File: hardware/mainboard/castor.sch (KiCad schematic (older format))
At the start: 41 parts, among them Q1 MMBT3904, U3 TL074, U4 74LVC2G74, U5 MCP6001-OT, U6 TL074

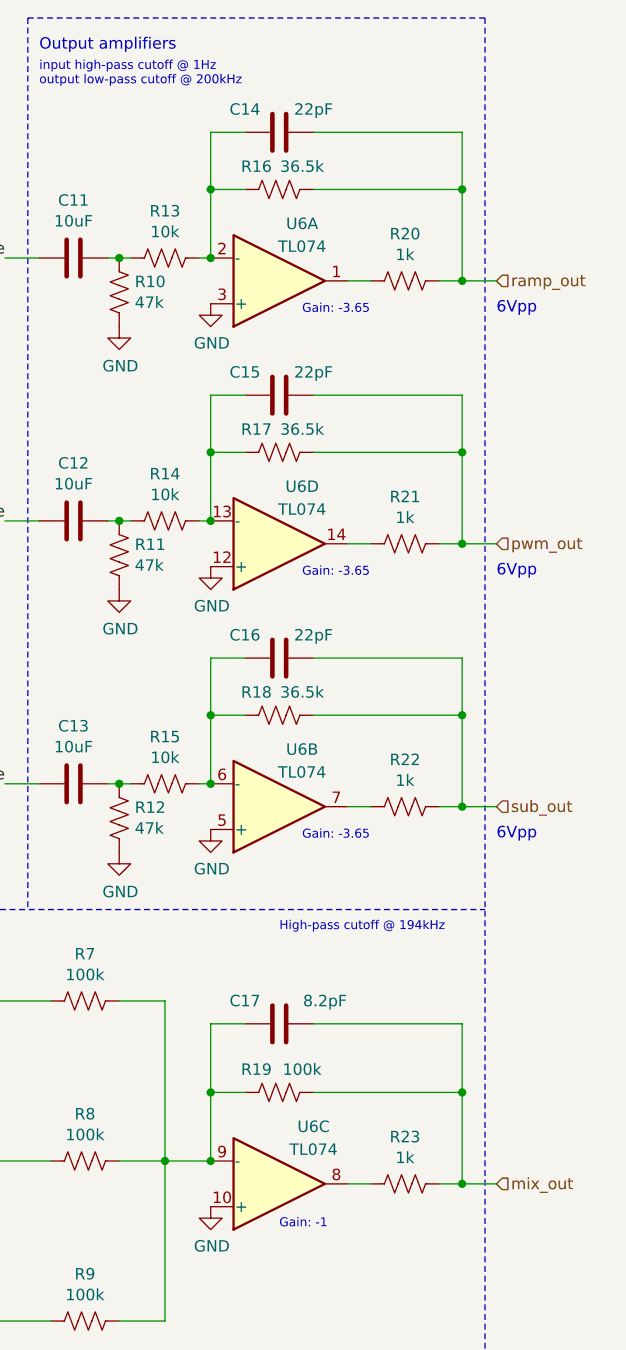
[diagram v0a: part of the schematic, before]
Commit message: Move output resistors outside of the feedback loop
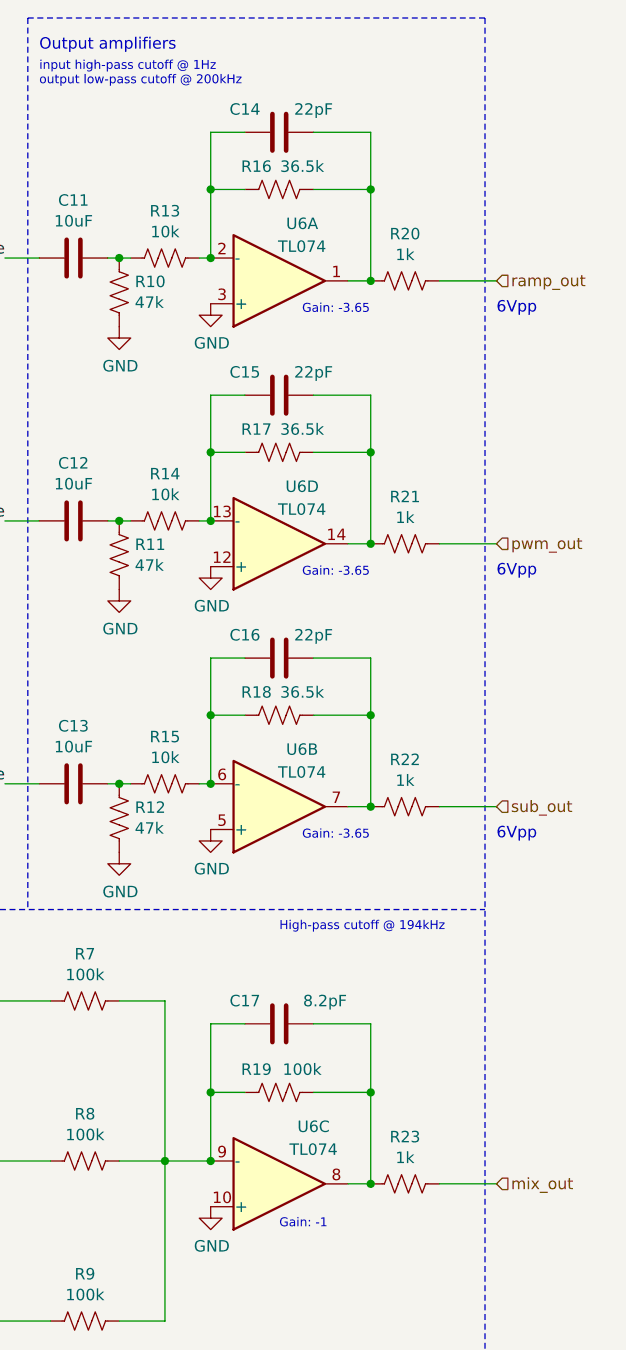
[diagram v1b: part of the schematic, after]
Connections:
- net mix_out: no longer C17.1, R19.2
- net pwm_out: no longer C15.1, R17.2
- net ramp_out: no longer C14.1, R16.2
- net sub_out: no longer C16.1, R18.2
- net at R20.1, U6.1: now also C14.1, R16.2
- net at R23.1, U6.8: now also C17.1, R19.2
- net at R21.1, U6.14: now also C15.1, R17.2
- net at R22.1, U6.7: now also C16.1, R18.2
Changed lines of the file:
@@
 	8550 5200 8700 5200
 Wire Wire Line
-	9000 5200 9650 5200
+	9000 5200 9250 5200
 $Comp
 L Device:R_US R7
@@
 $EndComp
 Wire Wire Line
-	9550 1650 9650 1650
-Wire Wire Line
 	8550 1550 8550 1250
 Wire Wire Line
@@
 Connection ~ 8550 1550
 Wire Wire Line
-	9000 1000 9650 1000
-Wire Wire Line
-	9650 1000 9650 1250
-Connection ~ 9650 1650
-Wire Wire Line
-	9650 1650 9800 1650
+	9000 1000 9250 1000
 Wire Wire Line
 	8550 1250 8700 1250
@@
 	8550 1250 8550 1000
 Wire Wire Line
-	9000 1250 9650 1250
-Connection ~ 9650 1250
-Wire Wire Line
-	9650 1250 9650 1650
+	9000 1250 9250 1250
 $Comp
 L Device:C C12
@@
 $EndComp
 Wire Wire Line
-	9550 2800 9650 2800
-Wire Wire Line
 	8550 2700 8550 2400
 Wire Wire Line
@@
 Connection ~ 8550 2700
 Wire Wire Line
-	9000 2150 9650 2150
-Wire Wire Line
-	9650 2150 9650 2400
-Connection ~ 9650 2800
-Wire Wire Line
-	9650 2800 9800 2800
+	9000 2150 9250 2150
 Wire Wire Line
 	8550 2400 8700 2400
@@
 	8550 2400 8550 2150
 Wire Wire Line
-	9000 2400 9650 2400
-Connection ~ 9650 2400
-Wire Wire Line
-	9650 2400 9650 2800
+	9000 2400 9250 2400
 Wire Notes Line
 	9750 500  7750 500
@@
 Connection ~ 8550 5200
 Wire Wire Line
-	9000 4900 9650 4900
-Wire Wire Line
-	9650 4900 9650 5200
+	9000 4900 9250 4900
 Wire Wire Line
 	8550 5500 8550 5200
-Wire Wire Line
-	9550 5600 9650 5600
-Wire Wire Line
-	9650 5200 9650 5600
-Connection ~ 9650 5200
-Connection ~ 9650 5600
-Wire Wire Line
-	9650 5600 9800 5600
 $Comp
 L power:GND #PWR016
@@
 	7750 500  7750 4400
 Wire Wire Line
-	9650 3550 9650 3950
-Connection ~ 9650 3550
-Wire Wire Line
-	9000 3550 9650 3550
+	9000 3550 9250 3550
 Wire Wire Line
 	8550 3550 8550 3300
@@
 	8550 3550 8700 3550
 Wire Wire Line
-	9650 3950 9800 3950
-Connection ~ 9650 3950
-Wire Wire Line
-	9650 3300 9650 3550
-Wire Wire Line
-	9000 3300 9650 3300
+	9000 3300 9250 3300
 Connection ~ 8550 3850
 Wire Wire Line
@@
 Wire Wire Line
 	8550 3850 8550 3550
-Wire Wire Line
-	9550 3950 9650 3950
 $Comp
 L Amplifier_Operational:TL074 U6
@@
 Text Notes 2050 4700 0    50   ~ 0
 1mA (max, est)
+Wire Wire Line
+	9250 1650 9250 1250
+Connection ~ 9250 1650
+Connection ~ 9250 1250
+Wire Wire Line
+	9250 1250 9250 1000
+Wire Wire Line
+	9550 1650 9800 1650
+Wire Wire Line
+	9250 2800 9250 2400
+Connection ~ 9250 2800
+Connection ~ 9250 2400
+Wire Wire Line
+	9250 2400 9250 2150
+Wire Wire Line
+	9550 2800 9800 2800
+Wire Wire Line
+	9250 3950 9250 3550
+Connection ~ 9250 3950
+Connection ~ 9250 3550
+Wire Wire Line
+	9250 3550 9250 3300
+Wire Wire Line
+	9550 3950 9800 3950
+Wire Wire Line
+	9250 5600 9250 5200
+Connection ~ 9250 5600
+Connection ~ 9250 5200
+Wire Wire Line
+	9250 5200 9250 4900
+Wire Wire Line
+	9550 5600 9800 5600
 $EndSCHEMATC

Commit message: Update mpns
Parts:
- C6, C9: mpn C0603C472F5GACTU -> C0603C472F3GECTU; mpn alt C0603C472F3GECTU -> C0603C472F5GACTU
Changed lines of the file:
@@
 F 4 "C0G 1%" H 2350 1250 50  0001 C CNN "Reqs"
 F 5 "yes" H 2350 1250 50  0001 C CNN "finalized"
-F 6 "C0603C472F5GACTU" H 2350 1250 50  0001 C CNN "mpn"
+F 6 "C0603C472F3GECTU" H 2350 1250 50  0001 C CNN "mpn"
 F 7 "1%, 50v" H 2350 1250 50  0001 C CNN "mpn specs"
-F 8 "C0603C472F3GECTU" H 2350 1250 50  0001 C CNN "mpn alt"
+F 8 "C0603C472F5GACTU" H 2350 1250 50  0001 C CNN "mpn alt"
 	1    2350 1250
 	0    1    1    0
@@
 F 4 "C0G 1%" H 3300 2500 50  0001 C CNN "Reqs"
 F 5 "yes" H 3300 2500 50  0001 C CNN "finalized"
-F 6 "C0603C472F5GACTU" H 3300 2500 50  0001 C CNN "mpn"
+F 6 "C0603C472F3GECTU" H 3300 2500 50  0001 C CNN "mpn"
 F 7 "1%, 50v" H 3300 2500 50  0001 C CNN "mpn specs"
-F 8 "C0603C472F3GECTU" H 3300 2500 50  0001 C CNN "mpn alt"
+F 8 "C0603C472F5GACTU" H 3300 2500 50  0001 C CNN "mpn alt"
 	1    3300 2500
 	0    1    1    0
